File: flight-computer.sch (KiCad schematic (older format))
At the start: 19 parts

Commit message: Progress on pinouts and STM32L433
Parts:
- removed U?: TMP102, symbol flight-computer:TMP102
- removed U?: BNO055, Package_LGA:LGA-28_5.2x3.8mm_P0.5mm, symbol Sensor_Motion:BNO055
- added C? (x2): 1uF, symbol Device:C_Small
- added C?: 0.1uF, symbol Device:C_Small
- added C? (x3): C_Small, symbol Device:C_Small
- added D?: GREEN, symbol Device:LED
- added D? (x3): SS14FL, symbol Device:D_Schottky_Small_ALT
- added D?: BLUE, symbol Device:LED
- added D?: RED, symbol Device:LED
- added J?: Throttle/BEC, symbol Connector_Generic:Conn_01x03
- added J?: Servo 1, symbol Connector_Generic:Conn_01x03
- added J?: Servo 2, symbol Connector_Generic:Conn_01x03
- added J?: Servo 3, symbol Connector_Generic:Conn_01x03
- added J?: Servo 4, symbol Connector_Generic:Conn_01x03
- added J?: USB_C_Receptacle, symbol Connector:USB_C_Receptacle
- added J?: Programming Header, symbol Connector_Generic:Conn_02x03_Top_Bottom
- added J?: Breakout, symbol Connector_Generic:Conn_01x08
- added J?: Ext, symbol Connector_Generic:Conn_01x03
- added J?: External Power, symbol Connector_Generic:Conn_01x02
- added L?: BLM15PG100SN1D, symbol Device:Ferrite_Bead_Small
- added R? (x3): 2k, symbol Device:R_Small
- added R? (x2): 5.1k, symbol Device:R_Small
- added R? (x2): 10k, symbol Device:R_Small
- added R? (x2): 4.7k, symbol Device:R_Small
- added RN?: EXB-24V220JX, symbol Device:R_Pack02
- added U?: NCV8161, symbol flight-computer:NCV8161
- added U?: Teensy3.6, symbol teensy:Teensy3.6
- added U?: TMP102, symbol flight-computer:TMP102
- C? (x10): symbol Device:C -> Device:C_Small
- R?: symbol Device:R -> Device:R_Small
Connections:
- net labels added: ALERT, D+, D-, EXT, SCL, SDA, SER1, SER2, SER3, SER4, SWCLK, SWDIO, THR, VBEC, VBUS, VEXT, VIN
- net labels removed: ~GND
- wire segments 54 -> 139
- no-connect marks 0 -> 11
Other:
- moved on the sheet: C?, L?, R?, SW?, U?, Y?

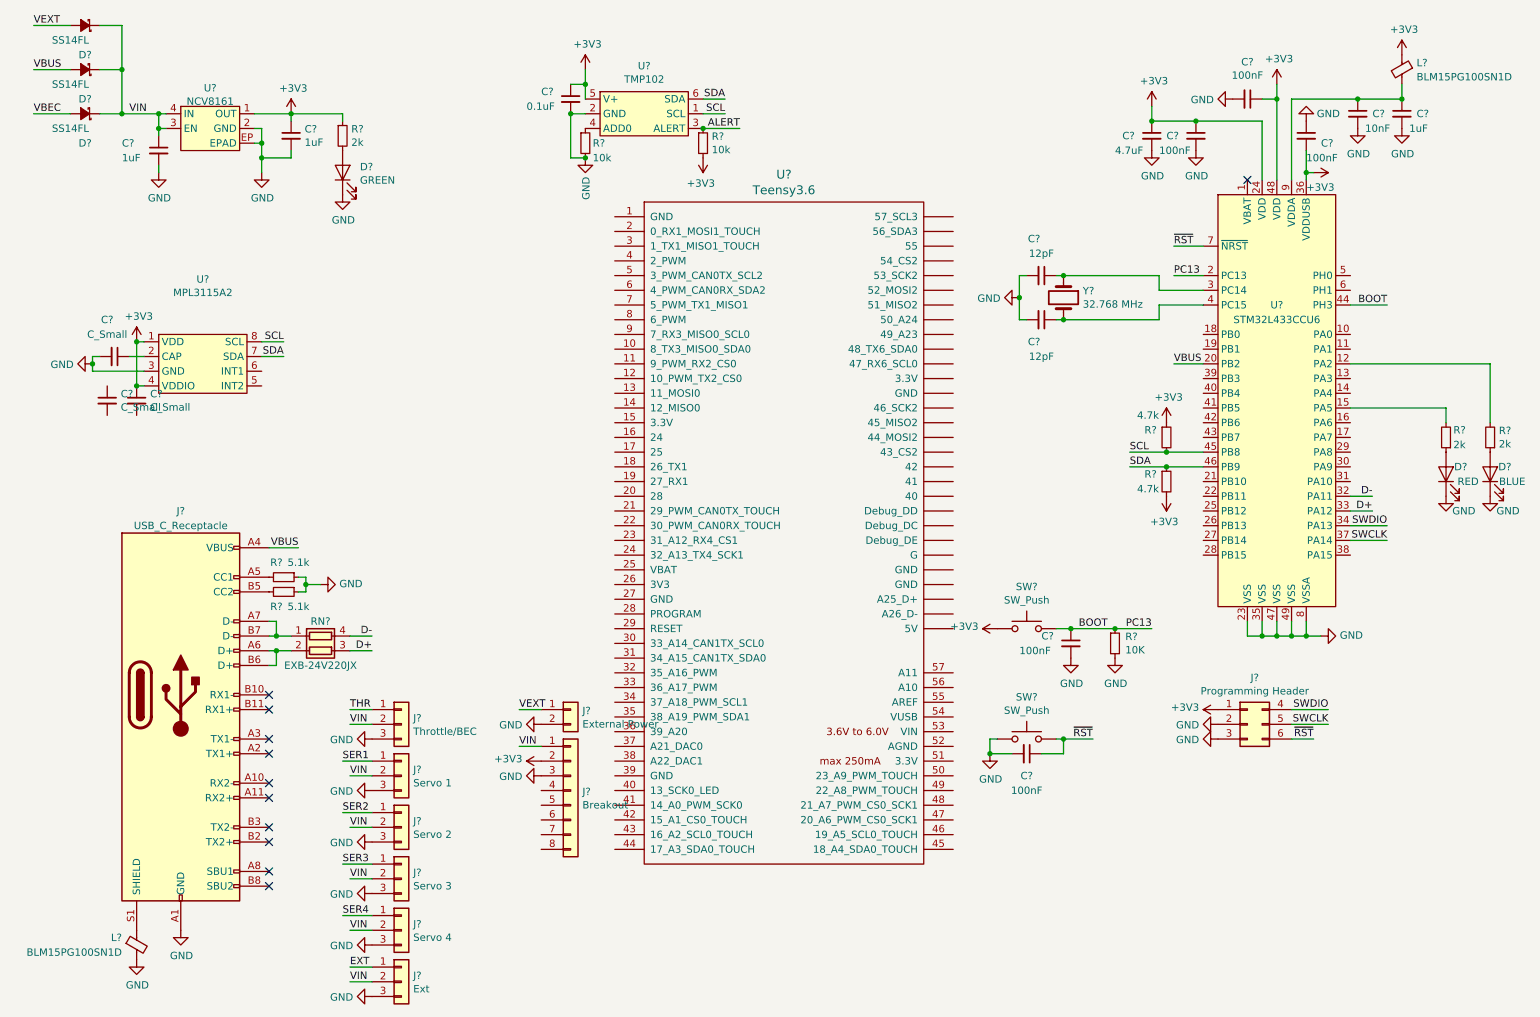
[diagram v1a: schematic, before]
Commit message: Teensy switched out as microcontroller
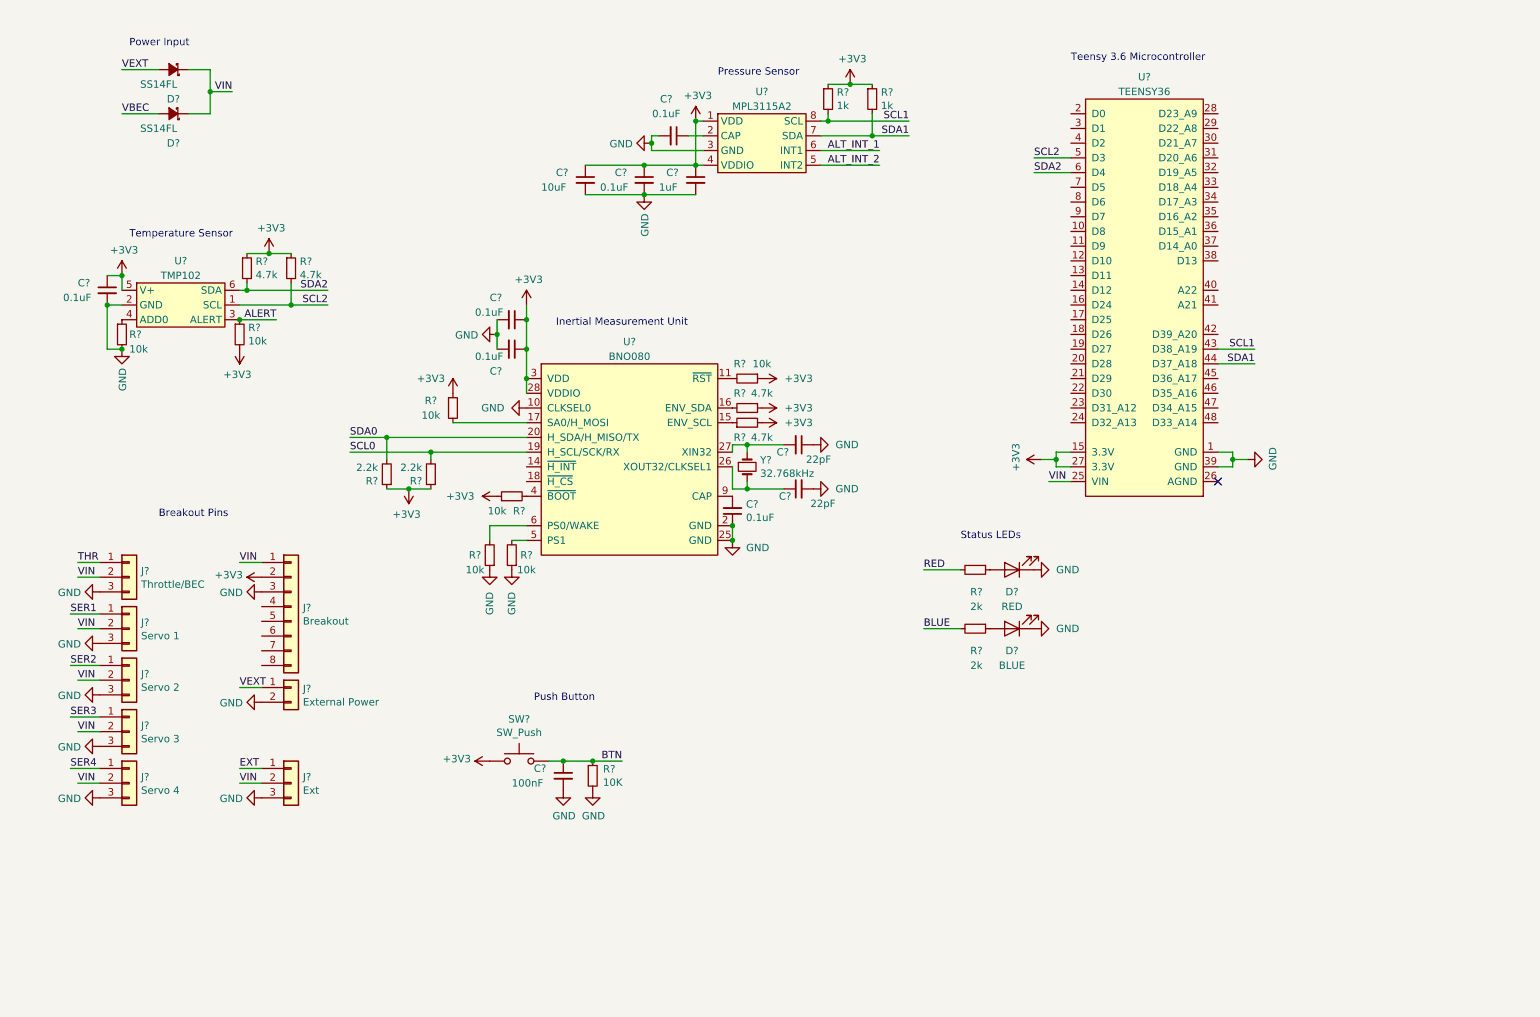
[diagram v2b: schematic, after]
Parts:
- removed C? (x2): 12pF, symbol Device:C_Small
- removed C?: 4.7uF, symbol Device:C_Small
- removed C? (x4): 100nF, symbol Device:C_Small
- removed C?: 10nF, symbol Device:C_Small
- removed C? (x3): 1uF, symbol Device:C_Small
- removed C?: C_Small, symbol Device:C_Small
- removed D?: GREEN, symbol Device:LED
- removed D?: SS14FL, symbol Device:D_Schottky_Small_ALT
- removed J?: USB_C_Receptacle, symbol Connector:USB_C_Receptacle
- removed J?: Programming Header, symbol Connector_Generic:Conn_02x03_Top_Bottom
- removed L? (x2): BLM15PG100SN1D, symbol Device:Ferrite_Bead_Small
- removed R?: 2k, symbol Device:R_Small
- removed R? (x2): 5.1k, symbol Device:R_Small
- removed R? (x2): 4.7k, symbol Device:R_Small
- removed RN?: EXB-24V220JX, symbol Device:R_Pack02
- removed SW?: SW_Push, symbol Switch:SW_Push
- removed U?: STM32L433CCU6, symbol flight-computer:STM32L433CCU6
- removed U?: NCV8161, symbol flight-computer:NCV8161
- removed U?: Teensy3.6, symbol teensy:Teensy3.6
- removed Y?: 32.768 MHz, symbol Device:Crystal
- added C? (x4): 0.1uF, symbol Device:C_Small
- added C?: 10uF, symbol Device:C_Small
- added C? (x2): 22pF, symbol Device:C_Small
- added R? (x4): 4.7k, symbol Device:R_Small
- added R? (x2): 1k, symbol Device:R_Small
- added R? (x5): 10k, symbol Device:R_Small
- added R? (x2): 2.2k, symbol Device:R_Small
- added U?: TEENSY36, symbol flight-computer:TEENSY36
- added U?: BNO080, symbol flight-computer:BNO080
- added Y?: 32.768kHz, symbol Device:Crystal_Small
- C?: value C_Small -> 0.1uF
- C?: value C_Small -> 1uF
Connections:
- net +3V3: now also C?.1, C?.1, C?.1, C?.1, R?.1, R?.1, R?.1, R?.1, R?.1, R?.1, R?.1, R?.1, R?.1, R?.1, R?.2, U?.15 (3.3V), U?.27 (3.3V), U?.28 (VDDIO), U?.3 (VDD)
- net GND: now also C?.2, C?.1, C?.1, C?.2, C?.2, C?.2, C?.2, C?.2, R?.1, R?.1, U?.1 (GND), U?.10 (CLKSEL0), U?.2 (GND), U?.25 (GND), U?.39 (GND)
- net VIN: now also U?.25 (VIN)
- net BLUE: now reaches R?.2
- net RED: now reaches R?.2
- net ALT_INT_2: now reaches U?.5 (INT2)
- net ALT_INT_1: now reaches U?.6 (INT1)
- net BOOT renamed BTN
- net SCL renamed SCL1
- net SCL1: now also R?.2, U?.43 (D38_A19); no longer U?.1 (SCL)
- net SDA renamed SDA1
- net SDA1: now also R?.2, U?.44 (D37_A18); no longer U?.6 (SDA)
- new net: R?.2, U?.11 (~RST)
- new net: R?.1, U?.15 (ENV_SCL)
- new net: R?.2, U?.16 (ENV_SDA)
- new net: R?.2, U?.17 (SA0/H_MOSI)
- new net: C?.1, U?.26 (XOUT32/CLKSEL1), Y?.2
- new net: C?.2, U?.27 (XIN32), Y?.1
- new net: R?.2, U?.4 (~BOOT)
- new net: R?.2, U?.5 (PS1)
- new net: R?.2, U?.6 (PS0/WAKE)
- new net: C?.2, U?.9 (CAP)
- new net SCL0: R?.2, U?.19 (H_SCL/SCK/RX)
- new net SCL2: R?.2, U?.1 (SCL), U?.5 (D3)
- new net SDA0: R?.2, U?.20 (H_SDA/H_MISO/TX)
- new net SDA2: R?.2, U?.6 (D4), U?.6 (SDA)
- no-connect marks 11 -> 1
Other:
- note added: "Breakout Pins"
- note added: "Inertial Measurement Unit"
- note added: "Power Input"
- note added: "Pressure Sensor"
- note added: "Push Button"
- note added: "Status LEDs"
- note added: "Teensy 3.6 Microcontroller"
- note added: "Temperature Sensor"
- moved on the sheet: C?, D?, J?, R?, SW?, U?

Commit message: Finished layout and annotation
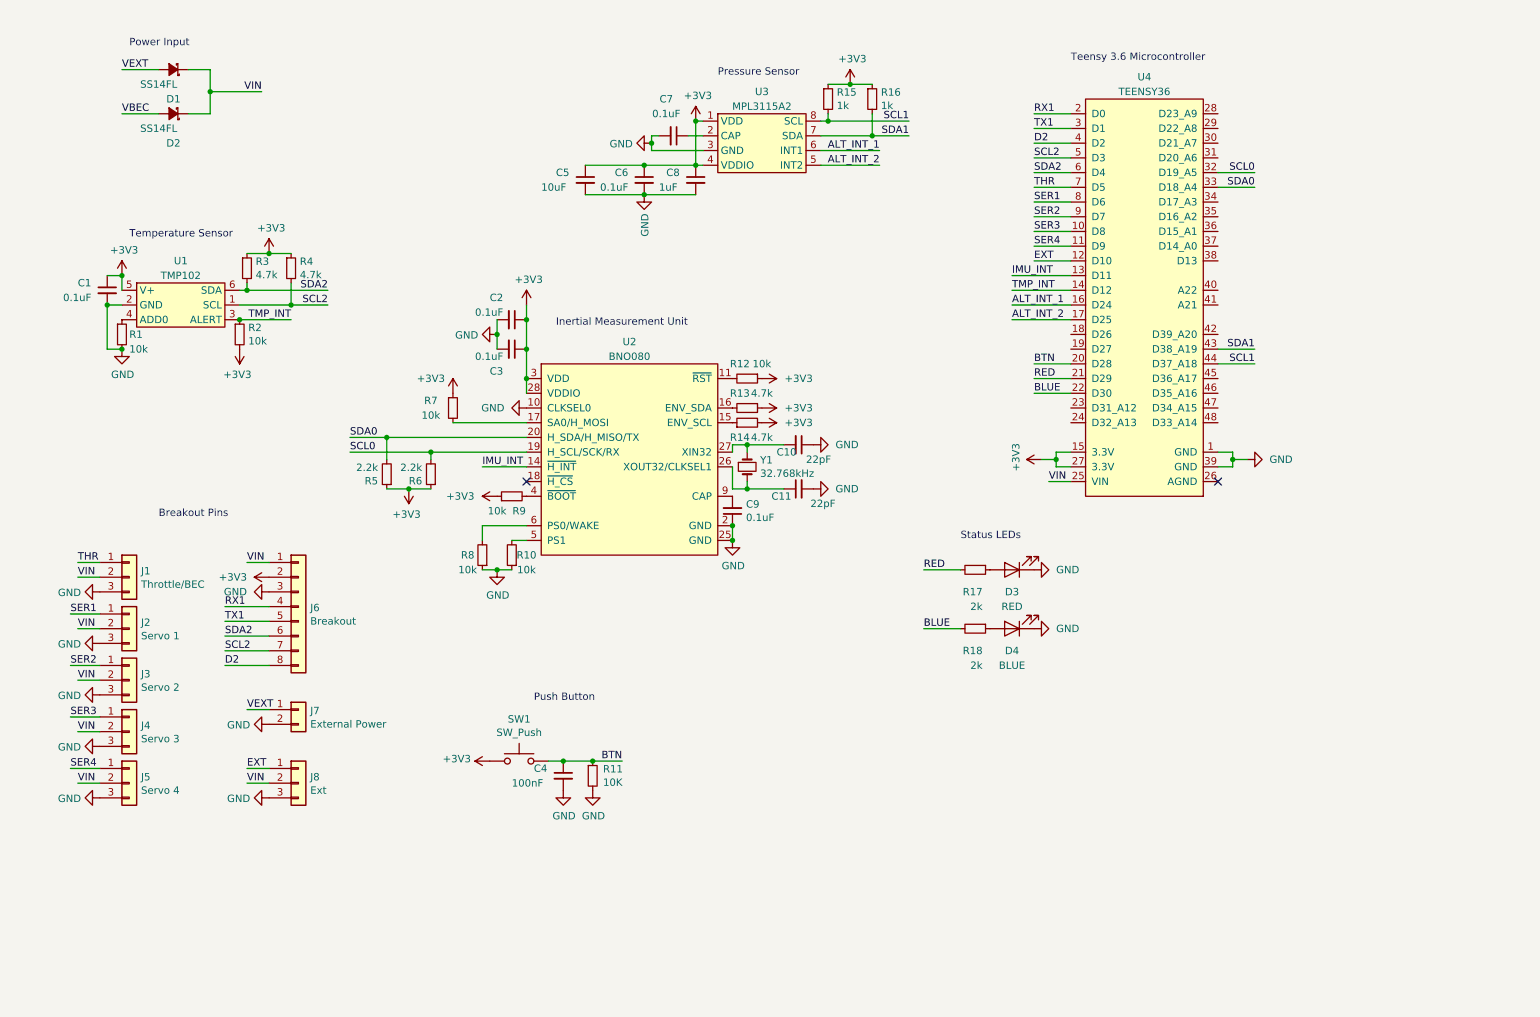
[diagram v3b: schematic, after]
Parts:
- gave numbers to parts that had none: 47
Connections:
- net ALERT is gone; now on net TMP_INT: R2.1, U1.3 (ALERT)
- net ALT_INT_1: now also U4.16 (D24)
- net ALT_INT_2: now also U4.17 (D25)
- net BLUE: now also U4.22 (D30)
- net BTN: now also U4.20 (D28)
- net EXT: now also U4.12 (D10)
- net RED: now also U4.21 (D29)
- net SCL0: now also U4.32 (D19_A5)
- net SCL1: now also U4.44 (D37_A18); no longer U4.43 (D38_A19)
- net SCL2: now also J6.7 (Pin_7)
- net SDA0: now also U4.33 (D18_A4)
- net SDA1: now also U4.43 (D38_A19); no longer U4.44 (D37_A18)
- net SDA2: now also J6.6 (Pin_6)
- net SER1: now also U4.8 (D6)
- net SER2: now also U4.9 (D7)
- net SER3: now also U4.10 (D8)
- net SER4: now also U4.11 (D9)
- net THR: now also U4.7 (D5)
- net IMU_INT: now reaches U4.13 (D11)
- net IMU_INT: now also U2.14 (~H_INT)
- net TMP_INT: now reaches U4.14 (D12)
- net RX1: now reaches U4.2 (D0)
- net RX1: now also J6.4 (Pin_4)
- net TX1: now reaches U4.3 (D1)
- net TX1: now also J6.5 (Pin_5)
- net D2: now reaches U4.4 (D2)
- net D2: now also J6.8 (Pin_8)
- no-connect marks 1 -> 2
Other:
- moved on the sheet: J6, J7, J8, R8

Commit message: Assigning footprints
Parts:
- U?: renamed from U3; footprint (none) -> Package_LGA:LGA-8_3x5mm_P1.25mm
- U?: renamed from U1; footprint (none) -> Package_TO_SOT_SMD:SOT-563
- U?: renamed from U2; footprint (none) -> Package_LGA:LGA-28_5.2x3.8mm_P0.5mm
- renumbered C4 to C?, C1 to C?, C6 to C?, C5 to C?, C9 to C?, C2 to C?, C3 to C?, C10 to C?, C11 to C?, C7 to C?, C8 to C?, D2 to D?, D4 to D?, D3 to D?, D1 to D?, J1 to J?, J2 to J?, J3 to J?, J4 to J?, J5 to J?, J6 to J?, J8 to J?, J7 to J?, R11 to R?, R3 to R?, R4 to R?, R18 to R?, R17 to R?, R1 to R?, R15 to R?, R16 to R?, R2 to R?, R12 to R?, R13 to R?, R14 to R?, R9 to R?, R7 to R?, R5 to R?, R6 to R?, R10 to R?, R8 to R?, SW1 to SW?, U4 to U?, Y1 to Y?

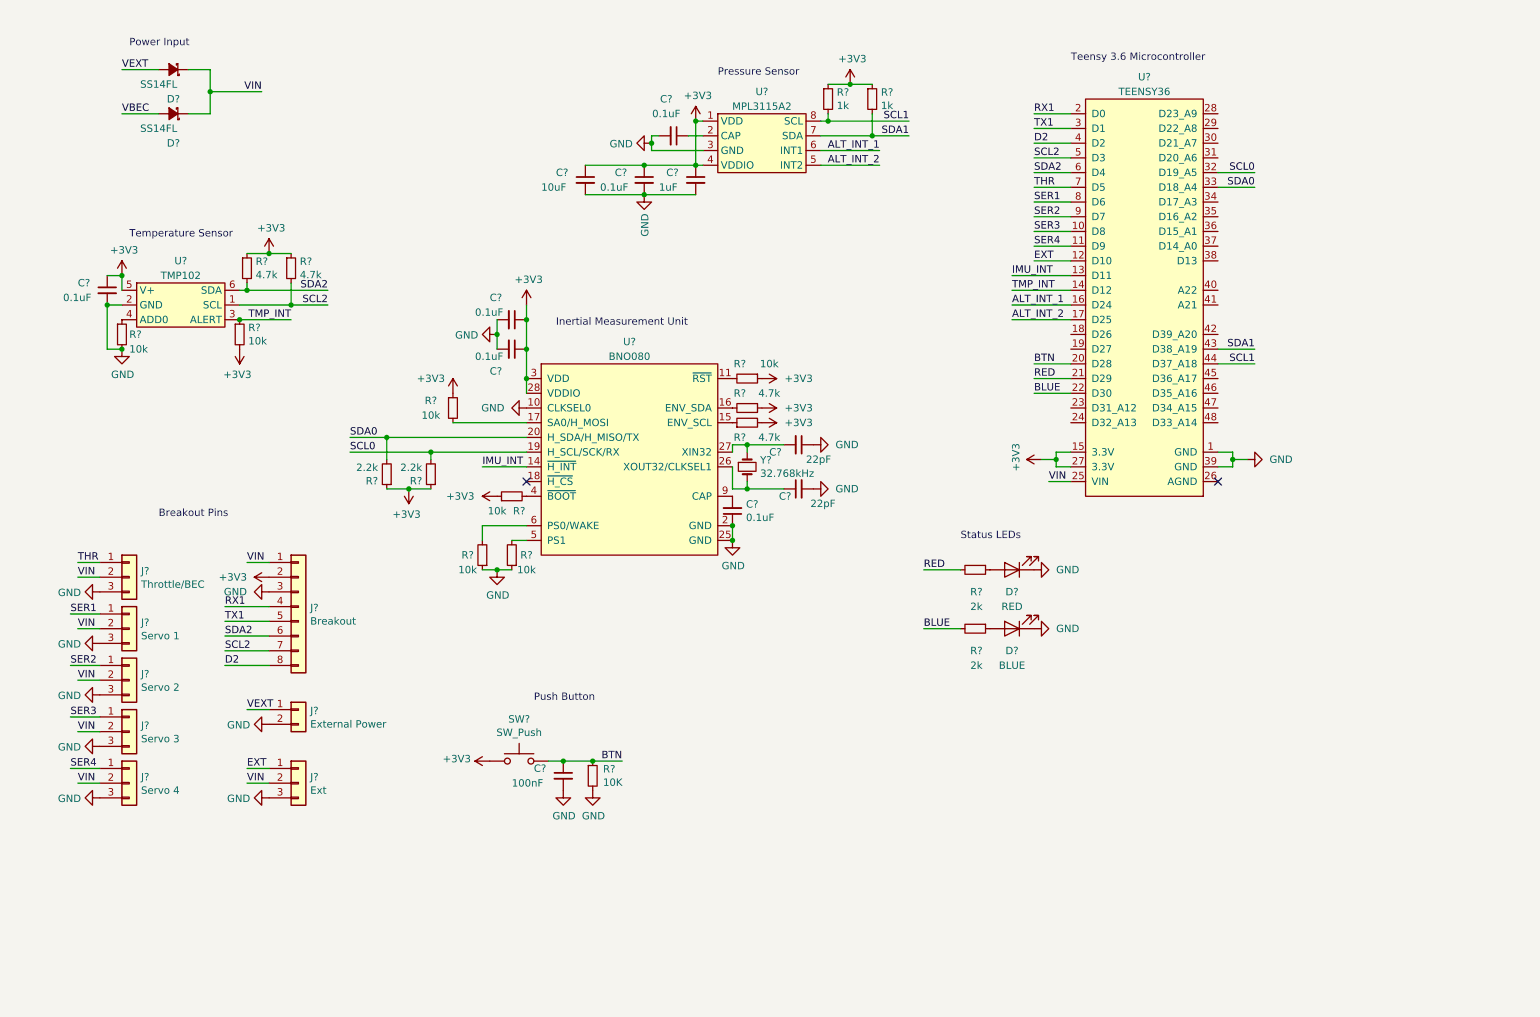
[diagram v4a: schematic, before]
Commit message: Created custom footprint library
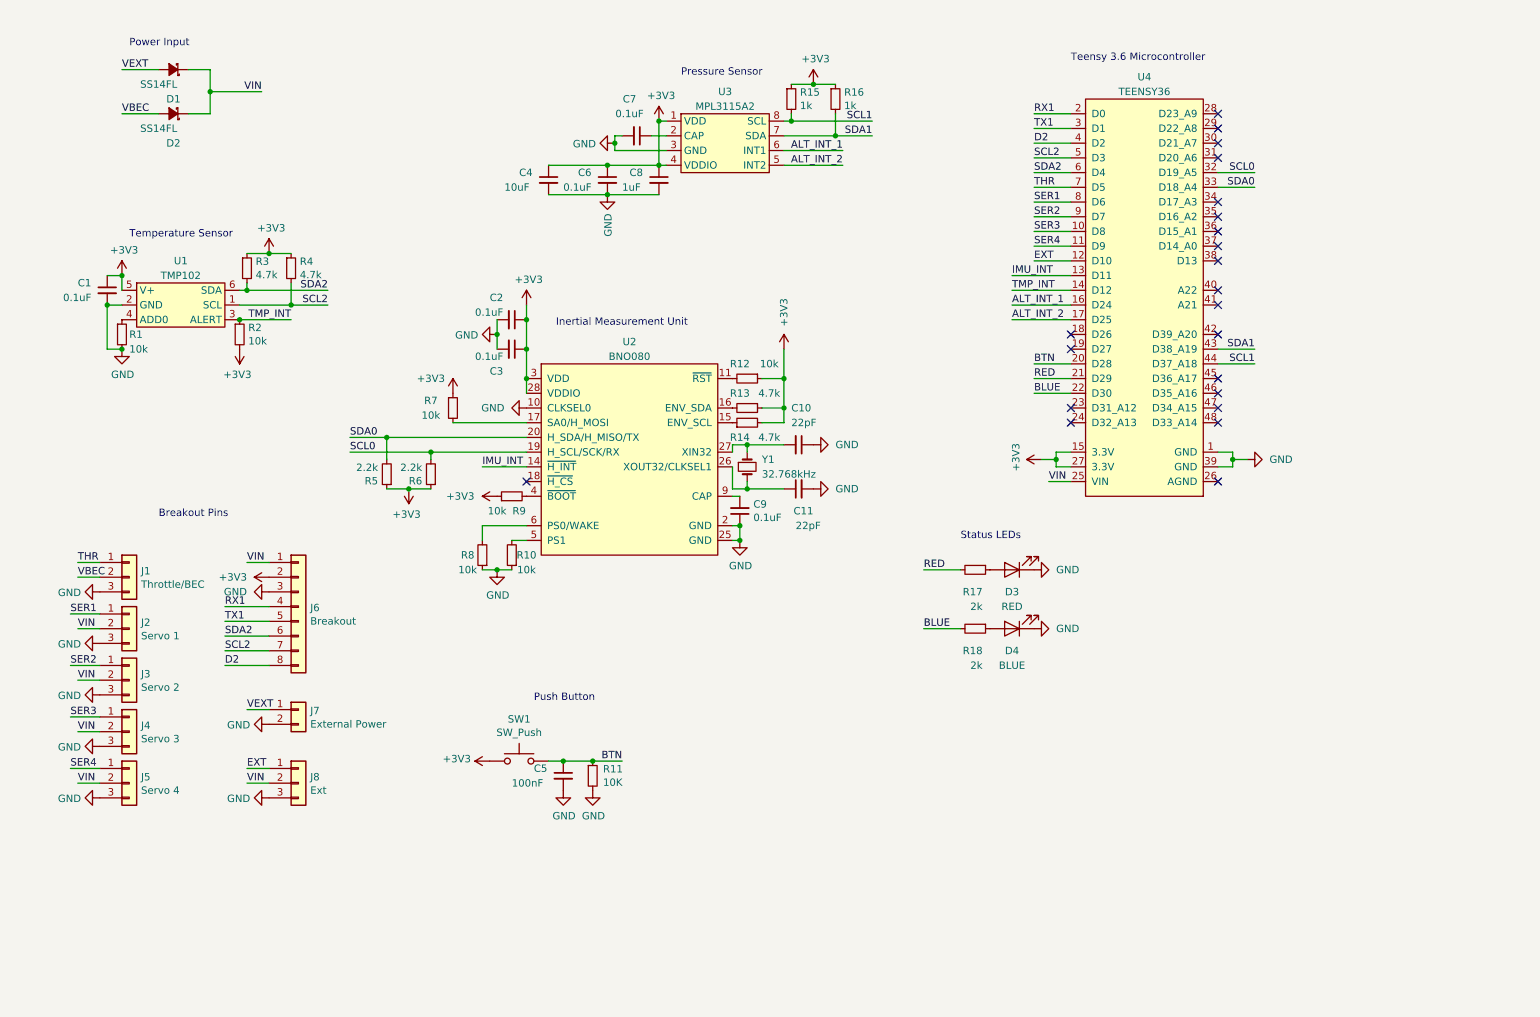
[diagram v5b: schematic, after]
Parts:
- removed SW?: SW_Push, symbol Switch:SW_Push
- added SW1: SW_Push, symbol Switch:SW_Push
- gave numbers to parts that had none: 46
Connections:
- net +3V3: now also SW1.1
- net BTN: now also SW1.2
- net VBEC: now also J1.2 (Pin_2)
- net VIN: no longer J1.2 (Pin_2)
- no-connect marks 2 -> 22
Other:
- moved on the sheet: C4, C6, C7, C8, C9, R15, R16, U3
